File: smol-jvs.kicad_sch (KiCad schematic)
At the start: 15 parts, among them J1 USB_B, J2 Misc, J3 Dips, J5 Power, J6 Controls, Q1 AO3400A, U1 ISL3175EIBZ-T, U2 Pico

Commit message: new gerbers and minor updates
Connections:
- net dip3: no longer U2.20 (GPIO15)
- no-connect marks 14 -> 15
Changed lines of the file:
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@@
   (junction (at 210.82 200.66) (diameter 0) (color 0 0 0 0)
   )
+  (no_connect (at 316.23 213.36))
   (no_connect (at 232.41 227.33))
   (no_connect (at 227.33 227.33))
@@
     (effects (font (size 1.27 1.27)) (justify left bottom))
   )
-  (label "dip3" (at 316.23 213.36 180)
-    (effects (font (size 1.27 1.27)) (justify right bottom))
-  )
   (label "jvs_de" (at 316.23 175.26 180)

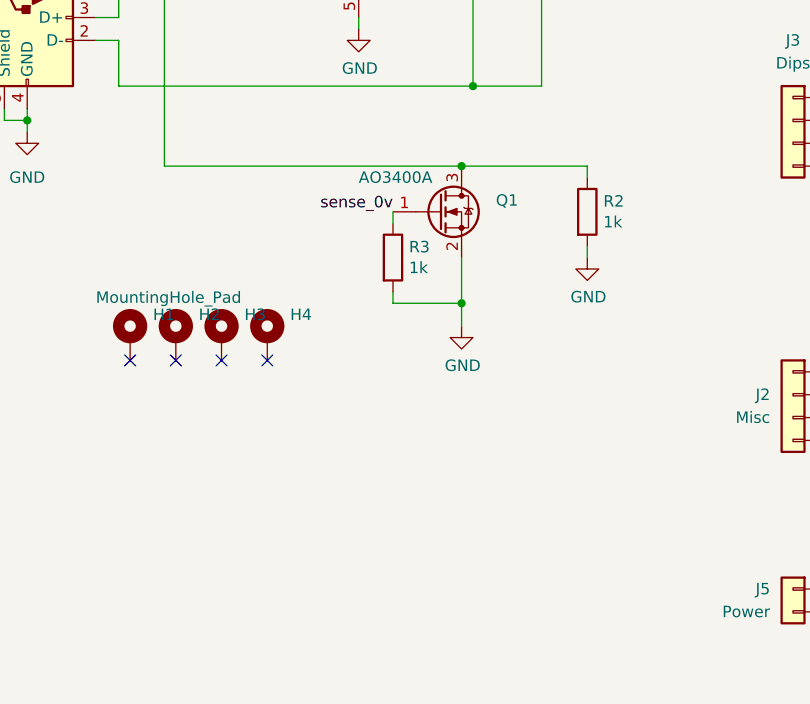
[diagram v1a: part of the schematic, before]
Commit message: Go back to using diodes for sense again
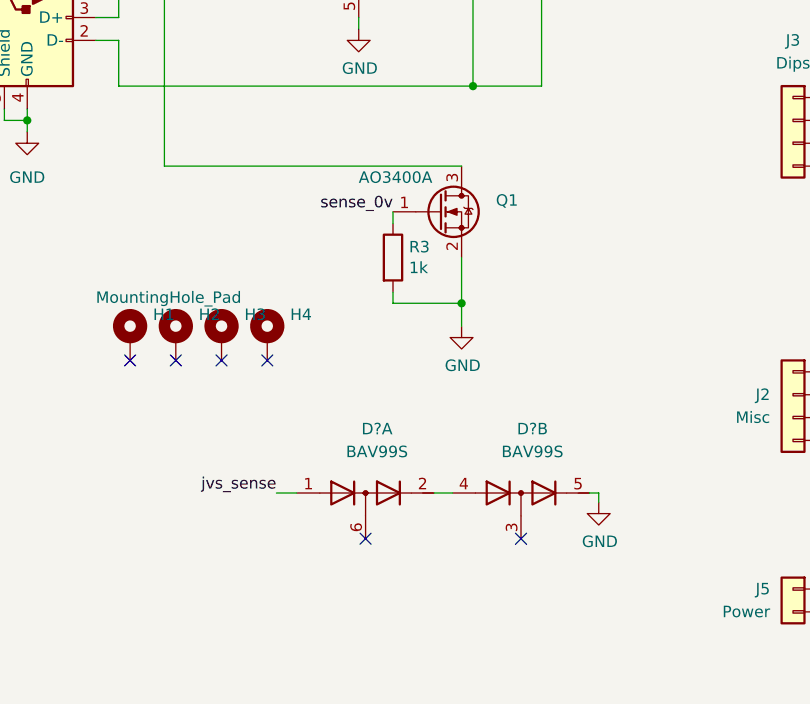
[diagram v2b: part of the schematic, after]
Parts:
- removed R2: 1k, Resistor_SMD:R_0805_2012Metric, symbol Device:R
- added D? (x2): BAV99S, Package_TO_SOT_SMD:SOT-363_SC-70-6, symbol Diode:BAV99S
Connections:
- net GND: now also D?.5 (K4)
- net jvs_sense: now also D?.1 (A1)
- new net: D?.2 (K2), D?.4 (A3)
- no-connect marks 15 -> 17
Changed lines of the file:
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@@
   (junction (at 260.35 196.85) (diameter 0) (color 0 0 0 0)
-  )
-  (junction (at 259.08 205.74) (diameter 0) (color 0 0 0 0)
   )
   (junction (at 259.08 220.98) (diameter 0) (color 0 0 0 0)
@@
   (no_connect (at 331.47 218.44))
   (no_connect (at 351.79 213.36))
+  (no_connect (at 265.684 247.142))
+  (no_connect (at 248.412 247.142))
   (wire (pts (xy 247.65 189.23) (xy 247.65 190.5))
     (stroke (width 0) (type default) (color 0 0 0 0))
@@
     (stroke (width 0) (type default) (color 0 0 0 0))
   )
-  (wire (pts (xy 273.05 205.74) (xy 273.05 207.01))
-    (stroke (width 0) (type default) (color 0 0 0 0))
-  )
   (wire (pts (xy 313.182 195.58) (xy 313.182 208.28))
     (stroke (width 0) (type default) (color 0 0 0 0))
@@
     (stroke (width 0) (type default) (color 0 0 0 0))
   )
-  (wire (pts (xy 273.05 205.74) (xy 259.08 205.74))
+  (wire (pts (xy 273.304 242.062) (xy 274.32 242.062))
     (stroke (width 0) (type default) (color 0 0 0 0))
   )
@@
     (stroke (width 0) (type default) (color 0 0 0 0))
   )
+  (wire (pts (xy 274.32 242.062) (xy 274.32 243.078))
+    (stroke (width 0) (type default) (color 0 0 0 0))
+  )
+  (wire (pts (xy 256.032 242.062) (xy 258.064 242.062))
+    (stroke (width 0) (type default) (color 0 0 0 0))
+  )
   (wire (pts (xy 300.99 252.73) (xy 302.26 252.73))
     (stroke (width 0) (type default) (color 0 0 0 0))
@@
     (stroke (width 0) (type default) (color 0 0 0 0))
   )
-  (wire (pts (xy 273.05 214.63) (xy 273.05 215.9))
-    (stroke (width 0) (type default) (color 0 0 0 0))
-  )
   (wire (pts (xy 229.87 184.15) (xy 237.49 184.15))
     (stroke (width 0) (type default) (color 0 0 0 0))
   )
+  (wire (pts (xy 238.506 242.062) (xy 240.792 242.062))
+    (stroke (width 0) (type default) (color 0 0 0 0))
+  )
   (wire (pts (xy 351.79 167.64) (xy 354.33 167.64))
     (stroke (width 0) (type default) (color 0 0 0 0))
@@
   )
   (label "jvs_tx" (at 237.49 184.15 180)
+    (effects (font (size 1.27 1.27)) (justify right bottom))
+  )
+  (label "jvs_sense" (at 238.506 242.062 180)
     (effects (font (size 1.27 1.27)) (justify right bottom))
   )
@@
     (pin "8")
   )
-  (symbol (lib_name "GND_6") (lib_id "power:GND") (at 273.05 215.9 0) (unit 1)
-    (in_bom yes) (on_board yes)
-    (property "Reference" "#PWR07" (id 0) (at 273.05 222.25 0)
-      (effects (font (size 1.27 1.27)) hide)
-    )
-    (property "Value" "GND" (id 1) (at 273.177 220.2942 0))
-    (property "Footprint" "" (id 2) (at 273.05 215.9 0)
-      (effects (font (size 1.27 1.27)) hide)
-    )
-    (property "Datasheet" "" (id 3) (at 273.05 215.9 0)
-      (effects (font (size 1.27 1.27)) hide)
-    )
-    (pin "1")
-  )
   (symbol (lib_id "Device:R") (at 251.46 215.9 0) (unit 1)
     (in_bom yes) (on_board yes)
@@
     )
     (property "Digikey" "311-10.0KCRCT-ND" (id 4) (at 251.46 215.9 0)
-      (effects (font (size 1.27 1.27)) hide)
-    )
-    (pin "1")
-    (pin "2")
-  )
-  (symbol (lib_id "Device:R") (at 273.05 210.82 0) (unit 1)
-    (in_bom yes) (on_board yes)
-    (property "Reference" "R2" (id 0) (at 274.828 209.6516 0)
-      (effects (font (size 1.27 1.27)) (justify left))
-    )
-    (property "Value" "1k" (id 1) (at 274.828 211.963 0)
-      (effects (font (size 1.27 1.27)) (justify left))
-    )
-    (property "Footprint" "Resistor_SMD:R_0805_2012Metric" (id 2) (at 271.272 210.82 90)
-      (effects (font (size 1.27 1.27)) hide)
-    )
-    (property "Datasheet" "~" (id 3) (at 273.05 210.82 0)
-      (effects (font (size 1.27 1.27)) hide)
-    )
-    (property "Digikey" "311-100CRCT-ND" (id 4) (at 273.05 210.82 0)
       (effects (font (size 1.27 1.27)) hide)
     )
@@
     )
     (pin "1")
+  )
+  (symbol (lib_id "Diode:BAV99S") (at 265.684 242.062 0) (unit 2)
+    (in_bom yes) (on_board yes) (fields_autoplaced)
+    (property "Reference" "D?" (id 0) (at 266.954 234.95 0))
+    (property "Value" "BAV99S" (id 1) (at 266.954 237.49 0))
+    (property "Footprint" "Package_TO_SOT_SMD:SOT-363_SC-70-6" (id 2) (at 265.684 254.762 0)
+      (effects (font (size 1.27 1.27)) hide)
+    )
+    (property "Datasheet" "https://assets.nexperia.com/documents/data-sheet/BAV99_SER.pdf" (id 3) (at 265.684 242.062 0)
+      (effects (font (size 1.27 1.27)) hide)
+    )
+    (pin "3")
+    (pin "4")
+    (pin "5")
   )
   (symbol (lib_name "GND_8") (lib_id "power:GND") (at 313.182 217.17 0) (unit 1)
@@
     (pin "1")
   )
+  (symbol (lib_id "Diode:BAV99S") (at 248.412 242.062 0) (unit 1)
+    (in_bom yes) (on_board yes) (fields_autoplaced)
+    (property "Reference" "D?" (id 0) (at 249.682 234.95 0))
+    (property "Value" "BAV99S" (id 1) (at 249.682 237.49 0))
+    (property "Footprint" "Package_TO_SOT_SMD:SOT-363_SC-70-6" (id 2) (at 248.412 254.762 0)
+      (effects (font (size 1.27 1.27)) hide)
+    )
+    (property "Datasheet" "https://assets.nexperia.com/documents/data-sheet/BAV99_SER.pdf" (id 3) (at 248.412 242.062 0)
+      (effects (font (size 1.27 1.27)) hide)
+    )
+    (pin "1")
+    (pin "2")
+    (pin "6")
+  )
   (symbol (lib_id "power:+3.3V") (at 330.2 237.49 0) (unit 1)
     (in_bom yes) (on_board yes)
@@
     )
     (property "Datasheet" "" (id 3) (at 304.8 205.74 0)
+      (effects (font (size 1.27 1.27)) hide)
+    )
+    (pin "1")
+  )
+  (symbol (lib_name "GND_6") (lib_id "power:GND") (at 274.32 243.078 0) (unit 1)
+    (in_bom yes) (on_board yes)
+    (property "Reference" "#PWR?" (id 0) (at 274.32 249.428 0)
+      (effects (font (size 1.27 1.27)) hide)
+    )
+    (property "Value" "GND" (id 1) (at 274.447 247.4722 0))
+    (property "Footprint" "" (id 2) (at 274.32 243.078 0)
+      (effects (font (size 1.27 1.27)) hide)
+    )
+    (property "Datasheet" "" (id 3) (at 274.32 243.078 0)
       (effects (font (size 1.27 1.27)) hide)
     )
@@
       (reference "#PWR06") (unit 1) (value "GND") (footprint "")
     )
-    (path "/00000000-0000-0000-0000-0000610daddf"
-      (reference "#PWR07") (unit 1) (value "GND") (footprint "")
-    )
     (path "/c83529f6-fced-4a22-919c-f3d53c20a55c"
       (reference "#PWR08") (unit 1) (value "GND") (footprint "")
@@
       (reference "#PWR020") (unit 1) (value "+3.3V") (footprint "")
     )
+    (path "/8f9f0312-a6da-44a7-9598-9e2034eb733d"
+      (reference "#PWR?") (unit 1) (value "GND") (footprint "")
+    )
+    (path "/728798fa-9d6f-4377-acf9-c914beeba9dd"
+      (reference "D?") (unit 1) (value "BAV99S") (footprint "Package_TO_SOT_SMD:SOT-363_SC-70-6")
+    )
+    (path "/3e6eed0e-55d3-494a-8d3d-99c26e038df5"
+      (reference "D?") (unit 2) (value "BAV99S") (footprint "Package_TO_SOT_SMD:SOT-363_SC-70-6")
+    )
     (path "/c6a072ba-7c6b-465b-bddf-f0c399477da0"
       (reference "H1") (unit 1) (value "MountingHole_Pad") (footprint "MountingHole:MountingHole_2.5mm_Pad")
@@
       (reference "R1") (unit 1) (value "120") (footprint "Resistor_SMD:R_0805_2012Metric")
     )
-    (path "/00000000-0000-0000-0000-00006110036c"
-      (reference "R2") (unit 1) (value "1k") (footprint "Resistor_SMD:R_0805_2012Metric")
-    )
     (path "/00000000-0000-0000-0000-0000610dcaea"

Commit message: Update smol-jvs.kicad_sch
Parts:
- gave numbers to parts that had none: 1
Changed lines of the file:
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@@
   (symbol (lib_id "Diode:BAV99S") (at 265.684 242.062 0) (unit 2)
     (in_bom yes) (on_board yes) (fields_autoplaced)
-    (property "Reference" "D?" (id 0) (at 266.954 234.95 0))
+    (property "Reference" "D1" (id 0) (at 266.954 234.95 0))
     (property "Value" "BAV99S" (id 1) (at 266.954 237.49 0))
     (property "Footprint" "Package_TO_SOT_SMD:SOT-363_SC-70-6" (id 2) (at 265.684 254.762 0)
@@
   (symbol (lib_id "Diode:BAV99S") (at 248.412 242.062 0) (unit 1)
     (in_bom yes) (on_board yes) (fields_autoplaced)
-    (property "Reference" "D?" (id 0) (at 249.682 234.95 0))
+    (property "Reference" "D1" (id 0) (at 249.682 234.95 0))
     (property "Value" "BAV99S" (id 1) (at 249.682 237.49 0))
     (property "Footprint" "Package_TO_SOT_SMD:SOT-363_SC-70-6" (id 2) (at 248.412 254.762 0)
@@
   (symbol (lib_name "GND_6") (lib_id "power:GND") (at 274.32 243.078 0) (unit 1)
     (in_bom yes) (on_board yes)
-    (property "Reference" "#PWR?" (id 0) (at 274.32 249.428 0)
+    (property "Reference" "#PWR0101" (id 0) (at 274.32 249.428 0)
       (effects (font (size 1.27 1.27)) hide)
     )
@@
     )
     (path "/8f9f0312-a6da-44a7-9598-9e2034eb733d"
-      (reference "#PWR?") (unit 1) (value "GND") (footprint "")
+      (reference "#PWR0101") (unit 1) (value "GND") (footprint "")
     )
     (path "/728798fa-9d6f-4377-acf9-c914beeba9dd"
-      (reference "D?") (unit 1) (value "BAV99S") (footprint "Package_TO_SOT_SMD:SOT-363_SC-70-6")
+      (reference "D1") (unit 1) (value "BAV99S") (footprint "Package_TO_SOT_SMD:SOT-363_SC-70-6")
     )
     (path "/3e6eed0e-55d3-494a-8d3d-99c26e038df5"
-      (reference "D?") (unit 2) (value "BAV99S") (footprint "Package_TO_SOT_SMD:SOT-363_SC-70-6")
+      (reference "D1") (unit 2) (value "BAV99S") (footprint "Package_TO_SOT_SMD:SOT-363_SC-70-6")
     )
     (path "/c6a072ba-7c6b-465b-bddf-f0c399477da0"

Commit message: Minor pcb updates + BOM
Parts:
- renumbered J6 to J4
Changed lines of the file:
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@@
   (symbol (lib_id "Connector_Generic:Conn_02x10_Odd_Even") (at 345.44 245.11 270) (unit 1)
     (in_bom yes) (on_board yes)
-    (property "Reference" "J6" (id 0) (at 330.2 245.1099 90)
+    (property "Reference" "J4" (id 0) (at 330.2 245.1099 90)
       (effects (font (size 1.27 1.27)) (justify right))
     )
@@
       (reference "J3") (unit 1) (value "Dips") (footprint "Connector_JST:JST_PH_B4B-PH-K_1x04_P2.00mm_Vertical")
     )
+    (path "/51cf508d-59ed-43ac-92da-b1be242395a6"
+      (reference "J4") (unit 1) (value "Controls") (footprint "Connector_PinHeader_2.54mm:PinHeader_2x10_P2.54mm_Vertical")
+    )
     (path "/c15c7b62-76a6-4348-946e-69a759a4b8e4"
       (reference "J5") (unit 1) (value "Power") (footprint "Connector_JST:JST_XH_B2B-XH-AM_1x02_P2.50mm_Vertical")
     )
-    (path "/51cf508d-59ed-43ac-92da-b1be242395a6"
-      (reference "J6") (unit 1) (value "Controls") (footprint "Connector_PinHeader_2.54mm:PinHeader_2x10_P2.54mm_Vertical")
-    )
     (path "/ae234909-6ebd-433f-aff9-a3ee2e1deb62"
